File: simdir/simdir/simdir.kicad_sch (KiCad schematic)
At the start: 16 parts, among them J4 Conn_02x05_Odd_Even, J5 Conn_Coaxial, J6 Conn_01x02, U58 LM2940CT-5.0

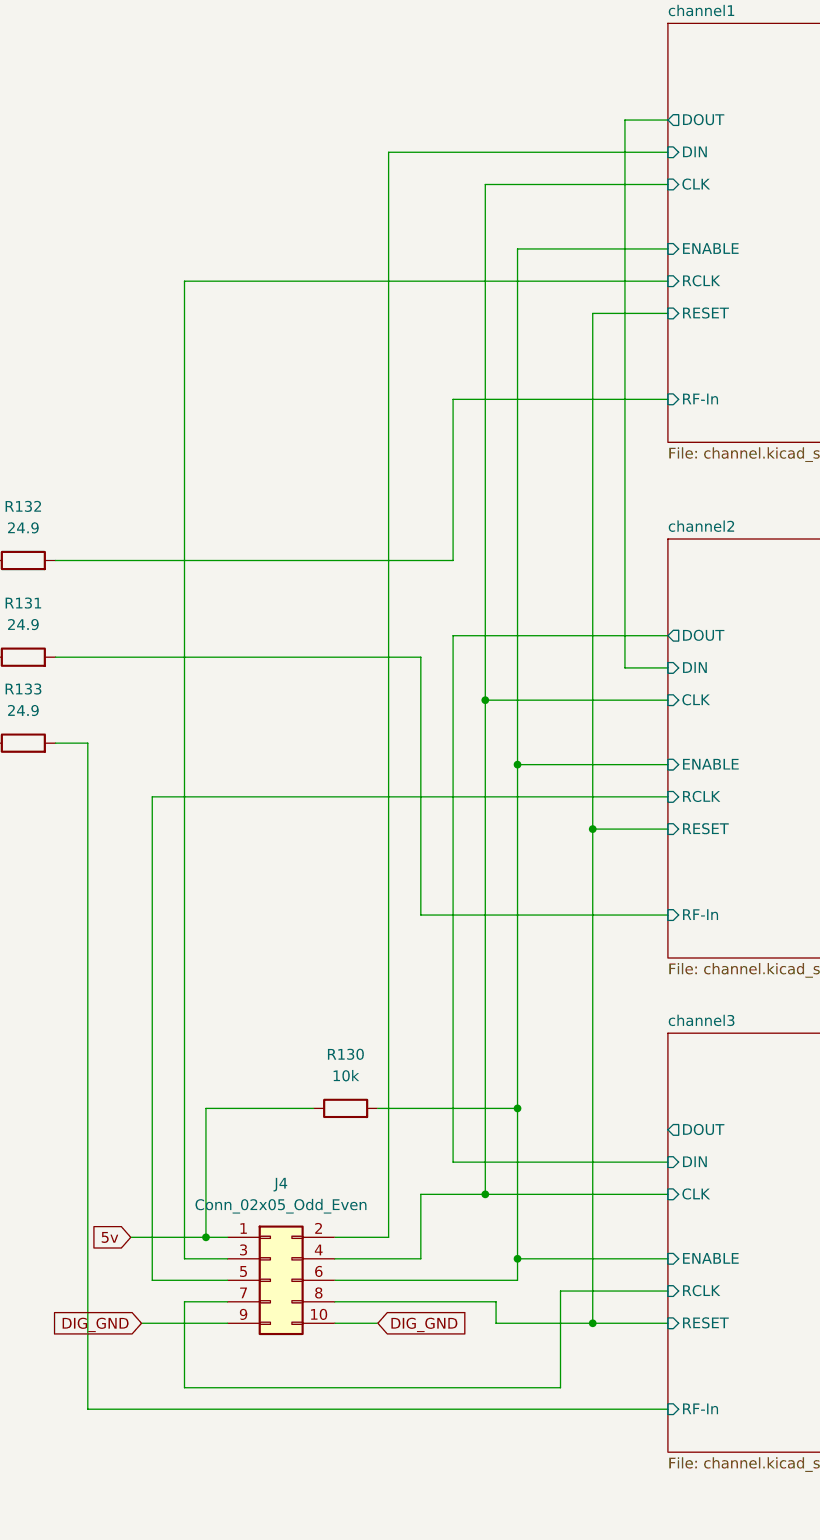
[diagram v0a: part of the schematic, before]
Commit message: Changed to 8-pin connector + added more ground planes.
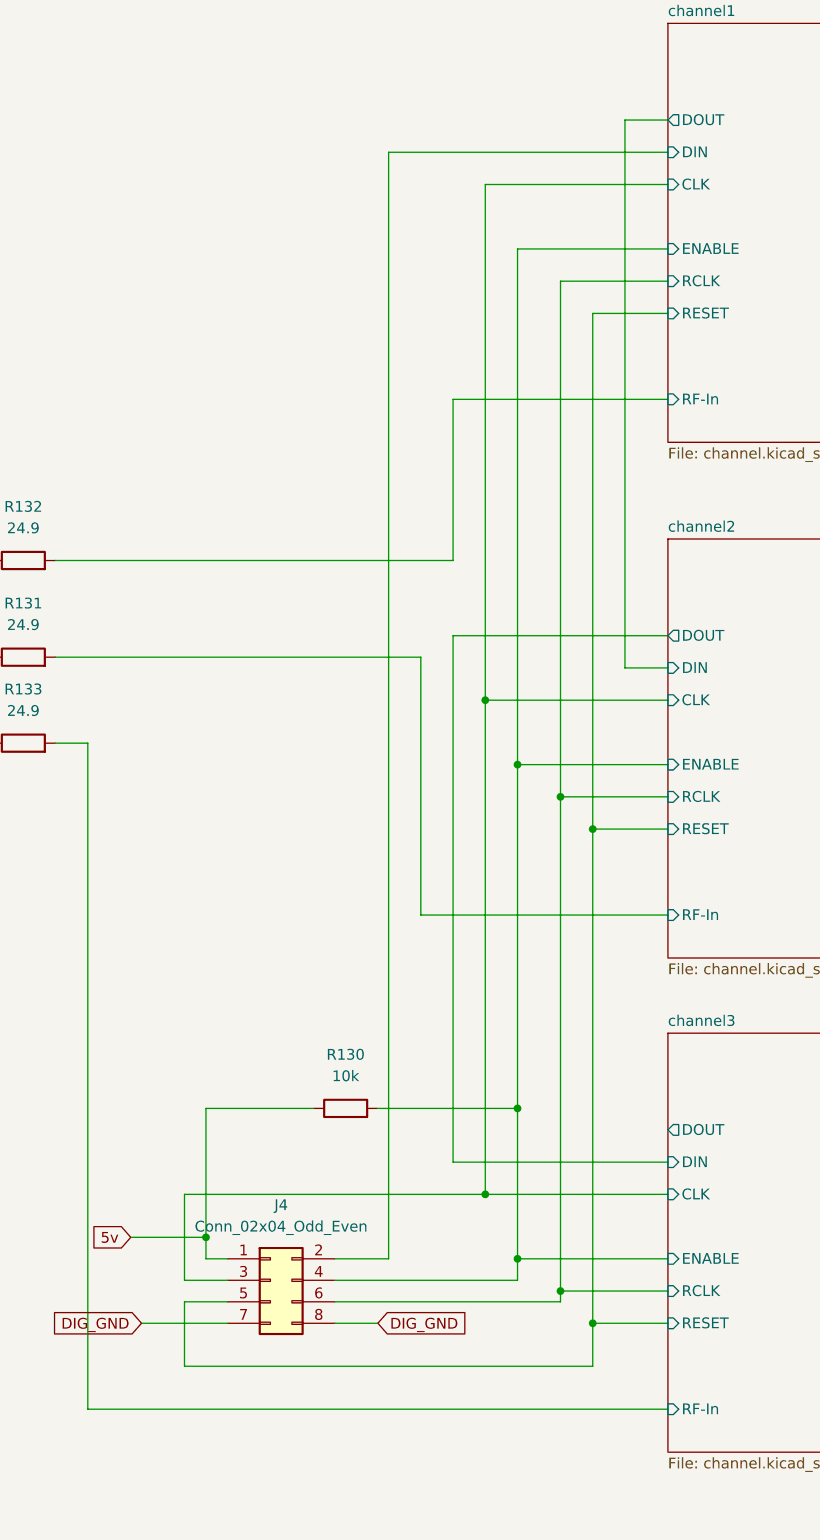
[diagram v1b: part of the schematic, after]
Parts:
- removed J4: Conn_02x05_Odd_Even, Connector_PinHeader_2.54mm:PinHeader_2x05_P2.54mm_Vertical, symbol Connector_Generic:Conn_02x05_Odd_Even
- added J4: Conn_02x04_Odd_Even, Connector_PinHeader_2.54mm:PinHeader_2x04_P2.54mm_Vertical, symbol Connector_Generic:Conn_02x04_Odd_Even
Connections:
- net 5v: now also J4.1 (Pin_1)
- net DIG_GND: now also J4.7 (Pin_7), J4.8 (Pin_8)
- net channel1/CLK: now also J4.3 (Pin_3)
- net channel1/DIN: now also J4.2 (Pin_2)
- net channel1/ENABLE: now also J4.4 (Pin_4)
- net channel1/RCLK: now also J4.6 (Pin_6)
- net channel1/RESET: now also J4.5 (Pin_5)
